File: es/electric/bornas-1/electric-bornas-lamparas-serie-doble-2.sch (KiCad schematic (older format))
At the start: 17 parts, among them X1 borna_12x2

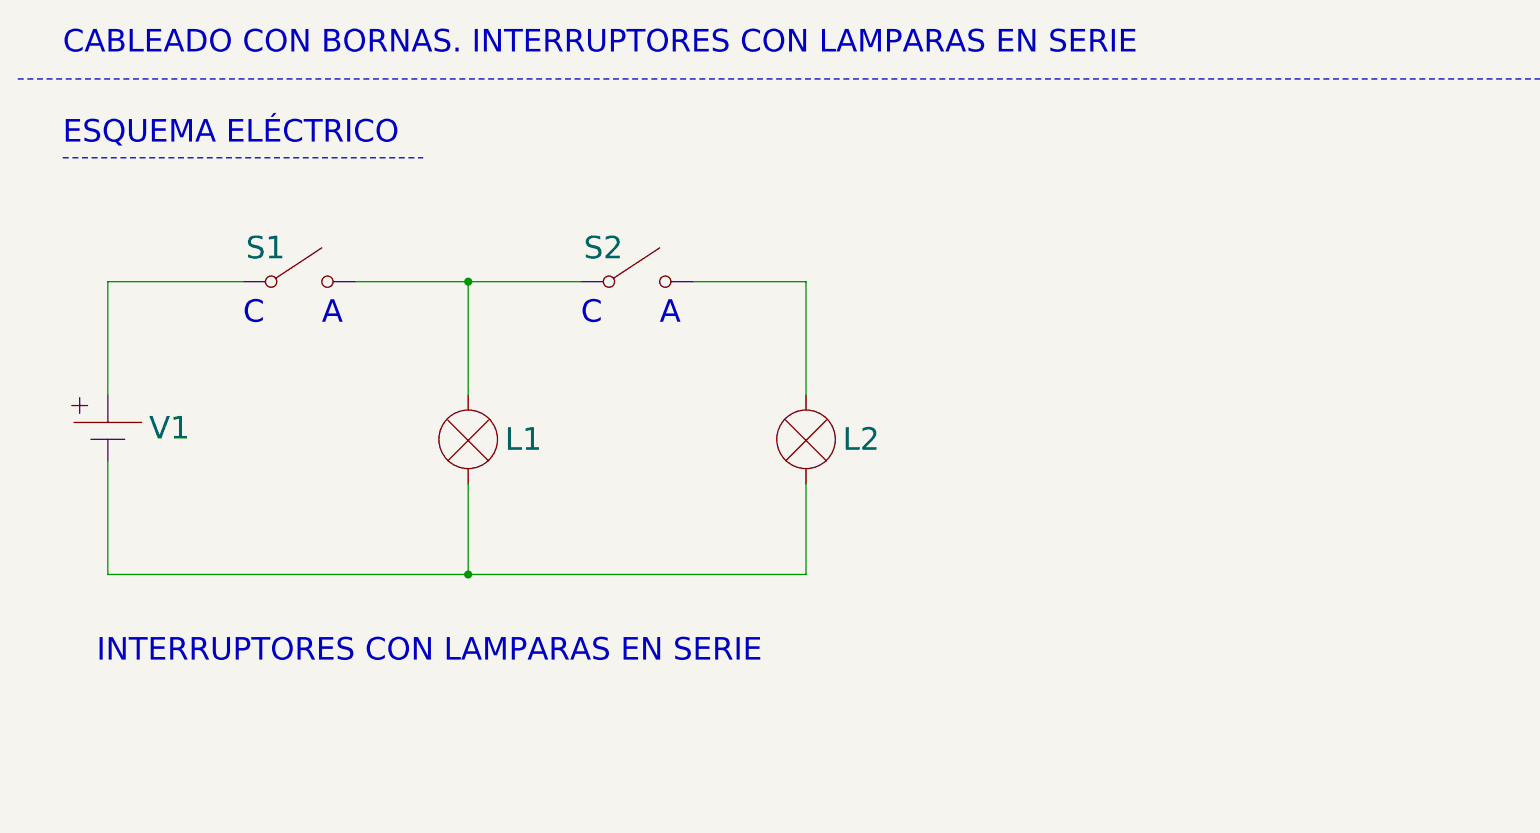
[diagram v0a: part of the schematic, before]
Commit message: Recompresión de imágenes y corrección ortográfica
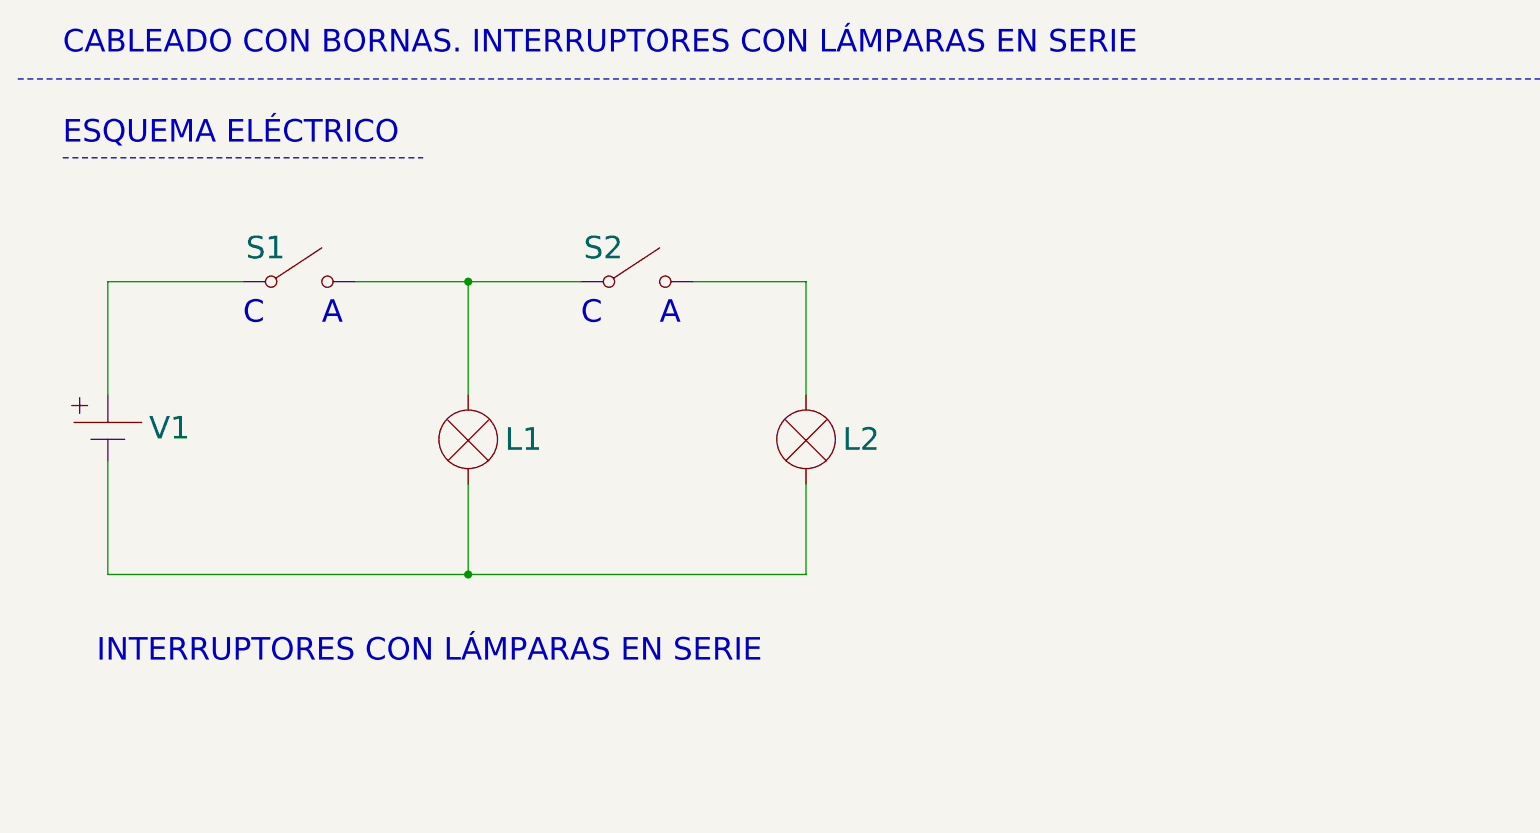
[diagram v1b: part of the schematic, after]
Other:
- note added: "CABLEADO CON BORNAS. INTERRUPTORES CON LÁMPARAS EN SERIE"
- note added: "INTERRUPTORES CON LÁMPARAS EN SERIE"
- note removed: "CABLEADO CON BORNAS. INTERRUPTORES CON LAMPARAS EN SERIE"
- note removed: "INTERRUPTORES CON LAMPARAS EN SERIE"
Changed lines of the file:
@@
 EESchema Schematic File Version 4
-LIBS:electric-bornas-lamparas-serie-doble-cache
-EELAYER 26 0
+EELAYER 30 0
 EELAYER END
 $Descr A4 8268 11693 portrait
@@
 $EndDescr
 Text Notes 400  500  0    100  ~ 0
-CABLEADO CON BORNAS. INTERRUPTORES CON LAMPARAS EN SERIE
+CABLEADO CON BORNAS. INTERRUPTORES CON LÁMPARAS EN SERIE
 $Comp
 L simbolos:CopyRight CP1
@@
 $EndComp
 Text Notes 550  3200 0    100  ~ 0
-INTERRUPTORES CON LAMPARAS EN SERIE
+INTERRUPTORES CON LÁMPARAS EN SERIE
 $Comp
 L simbolos:borna_6x2 X?
